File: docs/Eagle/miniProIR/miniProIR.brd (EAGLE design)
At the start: 61.2 x 31.8 mm, 14 parts, among them J4 Pixel, J7 Interface

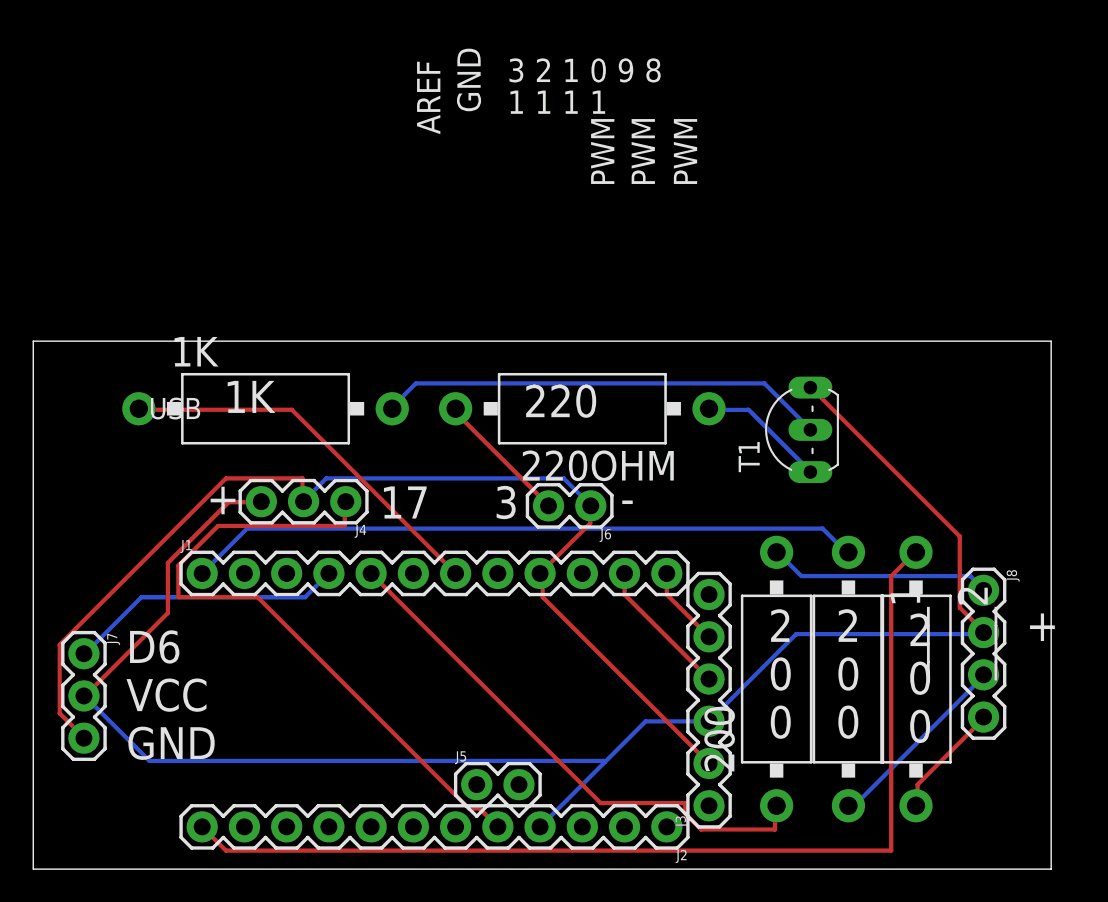
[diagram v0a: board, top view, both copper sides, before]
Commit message: Added spider/biped assembly
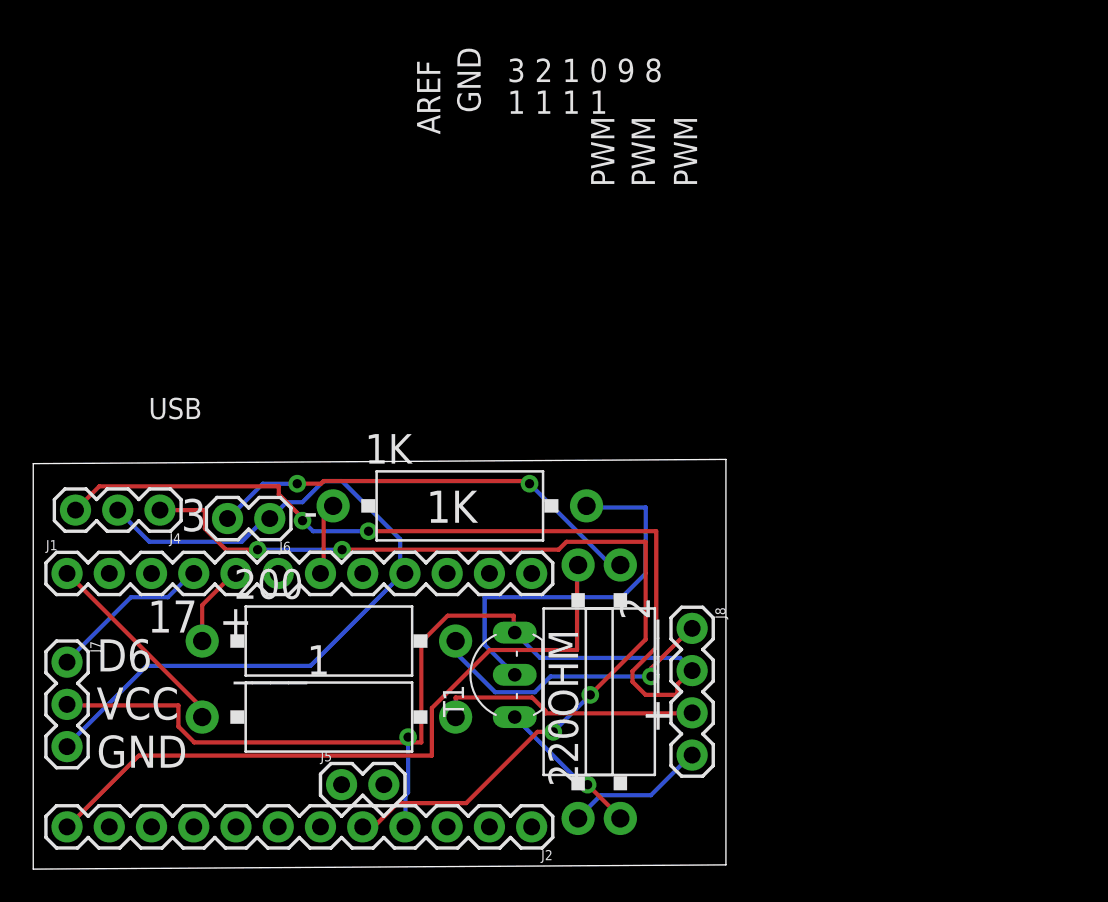
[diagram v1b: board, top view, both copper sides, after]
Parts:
- removed J3: (no value), SparkFun-Connectors:1X06
- moved ____1 31.3 mm to (17.8, 9.14), turned to 0 degrees
- moved 200 27.0 mm to (17.8, 13.7), turned to 0 degrees
- moved T1 23.1 mm to (27.7, 11.7)
- moved ____2 20.3 mm to (32.8, 10.7)
- moved J6 19.3 mm to (14.2, 21.1)
- moved J8 17.7 mm to (39.6, 14.5)
- moved 220OHM 17.2 mm to (35.3, 10.7), turned to 90 degrees
- moved 1K 13.1 mm to (25.7, 21.8)
- moved J4 11.2 mm to (7.62, 21.6)
- moved J1 8.13 mm to (2.03, 17.8)
- moved J2 8.13 mm to (30.0, 2.54)
- moved J5 8.13 mm to (18.5, 5.08)
- moved J7 1.14 mm to (2.03, 12.4)
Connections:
- net D0_E: no longer J3.4
- net D1_E: no longer J3.5
- net GND_E: no longer J3.2
- net VCC_E: no longer J3.3
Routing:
- net D9_E: track 40.6 -> 12.0 mm
- net D5_E: track 32.6 -> 4.98 mm
- net A3_E: track 39.3 -> 58.6 mm, vias 0 -> 4
- net D3_E: track 23.2 -> 4.40 mm
- net D10_E: track 60.6 -> 41.9 mm
- net IROUT: track 8.15 -> 26.8 mm, vias 0 -> 2
- net GND_E: track 66.0 -> 47.8 mm
- net D0_E: track 8.45 -> 0.00 mm
- net D6_E: track 16.7 -> 9.86 mm
- net D1_E: track 4.86 -> 0.00 mm
- net N$4: track 11.4 -> 15.9 mm
- net VCC_E: track 100.8 -> 105.3 mm, vias 0 -> 3
- net N$3: track 13.4 -> 17.8 mm, vias 0 -> 1
- net N$2: track 27.0 -> 23.3 mm
- net N$5: track 7.07 -> 8.44 mm
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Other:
- board size 61.2 x 31.8 mm -> 41.7 x 24.6 mm
- board text removed: "2 0 0"
- board text removed: "220"

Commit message: hyo
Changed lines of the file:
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@@
 GND</text>
 <text x="23.622" y="20.828" size="1.9304" layer="121">1K</text>
-<text x="36.576" y="8.382" size="1.9304" layer="121">+</text>
+<text x="37.084" y="11.176" size="1.9304" layer="121">+</text>
 </plain>
 <attributes>
